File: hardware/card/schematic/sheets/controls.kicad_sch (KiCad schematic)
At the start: 12 parts, among them SW1 KMR211NG, SW10A EVP-AKE31A, SW10B EVP-AKE31A, SW2 KMR211NG, SW3 KMR211NG, SW4 KMR211NG, SW5 KMR211NG, SW6 KMR211NG, SW7 KMR211NG, SW8 KMR211NG, SW9 EVP-AKE31A

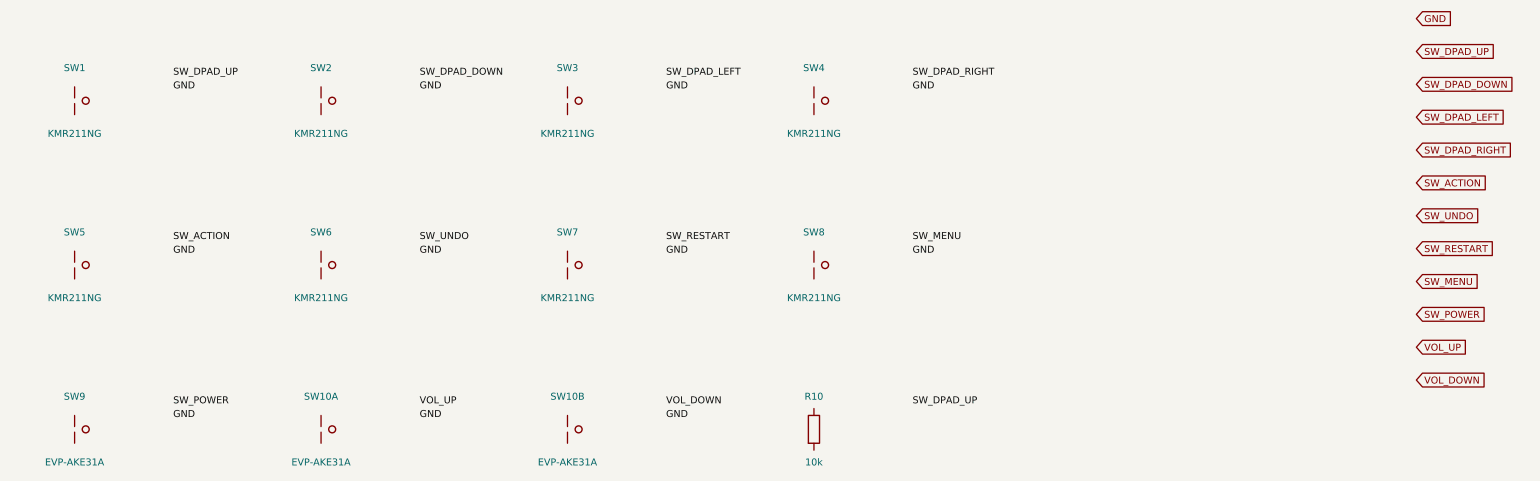
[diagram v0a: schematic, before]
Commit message: hardware: replace U7 power latch with a slide switch (hard off)
Owner-approved power model: top-edge SPDT slide switch gates the TPS63070
EN pin; hard off is the normal off (Game Boy/Arduboy style, ~1-1.5 s tuned
cold boot, end-of-level atomic saves). Deletes the U7 latch IC and SYSOFF
wiring, frees GPIO8, adds a VBUS-powered charge LED on BQ24075 CHG, and
demotes deep sleep to an optional idle battery-saver. Closes the U7
pre-route gate from the 2026-07-09 PCB review.

Co-authored-by: Cursor <cursoragent@cursor.com>
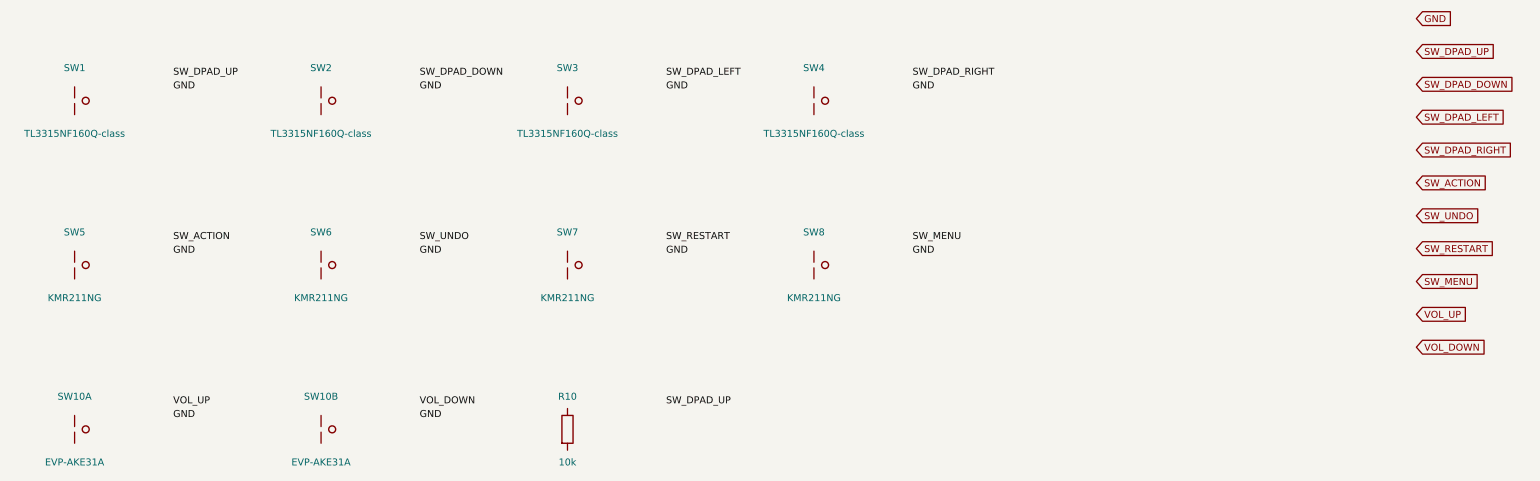
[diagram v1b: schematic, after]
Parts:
- removed SW9: EVP-AKE31A, TBD, symbol Switch:SW_Push
- SW1, SW2, SW3, SW4: value KMR211NG -> TL3315NF160Q-class
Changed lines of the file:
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@@
   (title_block
     (title "PuzzleScript Card — controls")
-    (date "2026-07-08")
+    (date "2026-07-09")
     (rev "spin1")
     (comment 1 "Auto-generated from connectivity.json")
@@
     (property "Reference" "SW1" (at 35 29 0)
       (effects (font (size 1.27 1.27))))
-    (property "Value" "KMR211NG" (at 35 41 0)
+    (property "Value" "TL3315NF160Q-class" (at 35 41 0)
       (effects (font (size 1.27 1.27))))
     (property "Footprint" "TBD" (at 35 35 0)
@@
     (property "Reference" "SW2" (at 80 29 0)
       (effects (font (size 1.27 1.27))))
-    (property "Value" "KMR211NG" (at 80 41 0)
+    (property "Value" "TL3315NF160Q-class" (at 80 41 0)
       (effects (font (size 1.27 1.27))))
     (property "Footprint" "TBD" (at 80 35 0)
@@
     (property "Reference" "SW3" (at 125 29 0)
       (effects (font (size 1.27 1.27))))
-    (property "Value" "KMR211NG" (at 125 41 0)
+    (property "Value" "TL3315NF160Q-class" (at 125 41 0)
       (effects (font (size 1.27 1.27))))
     (property "Footprint" "TBD" (at 125 35 0)
@@
     (property "Reference" "SW4" (at 170 29 0)
       (effects (font (size 1.27 1.27))))
-    (property "Value" "KMR211NG" (at 170 41 0)
+    (property "Value" "TL3315NF160Q-class" (at 170 41 0)
       (effects (font (size 1.27 1.27))))
     (property "Footprint" "TBD" (at 170 35 0)
@@
   (symbol (lib_id "Switch:SW_Push") (at 35 95 0) (unit 1)
     (exclude_from_sim no) (in_bom yes) (on_board yes) (dnp no) (fields_autoplaced)
-    (property "Reference" "SW9" (at 35 89 0)
+    (property "Reference" "SW10A" (at 35 89 0)
       (effects (font (size 1.27 1.27))))
     (property "Value" "EVP-AKE31A" (at 35 101 0)
@@
     (property "Datasheet" "~" (at 35 95 0)
       (effects (font (size 1.27 1.27)) hide))
-    (instances (project "card" (path "/card/sheets/controls" (reference "SW9") (unit 1))))
+    (instances (project "card" (path "/card/sheets/controls" (reference "SW10A") (unit 1))))
   )
   (label "GND" (at 53 92.5 0) (fields_autoplaced)
     (effects (font (size 1.27 1.27)) (justify left)))
-  (label "SW_POWER" (at 53 90 0) (fields_autoplaced)
+  (label "VOL_UP" (at 53 90 0) (fields_autoplaced)
     (effects (font (size 1.27 1.27)) (justify left)))
   (symbol (lib_id "Switch:SW_Push") (at 80 95 0) (unit 1)
     (exclude_from_sim no) (in_bom yes) (on_board yes) (dnp no) (fields_autoplaced)
-    (property "Reference" "SW10A" (at 80 89 0)
+    (property "Reference" "SW10B" (at 80 89 0)
       (effects (font (size 1.27 1.27))))
     (property "Value" "EVP-AKE31A" (at 80 101 0)
@@
     (property "Datasheet" "~" (at 80 95 0)
       (effects (font (size 1.27 1.27)) hide))
-    (instances (project "card" (path "/card/sheets/controls" (reference "SW10A") (unit 1))))
+    (instances (project "card" (path "/card/sheets/controls" (reference "SW10B") (unit 1))))
   )
   (label "GND" (at 98 92.5 0) (fields_autoplaced)
     (effects (font (size 1.27 1.27)) (justify left)))
-  (label "VOL_UP" (at 98 90 0) (fields_autoplaced)
-    (effects (font (size 1.27 1.27)) (justify left)))
-  (symbol (lib_id "Switch:SW_Push") (at 125 95 0) (unit 1)
-    (exclude_from_sim no) (in_bom yes) (on_board yes) (dnp no) (fields_autoplaced)
-    (property "Reference" "SW10B" (at 125 89 0)
-      (effects (font (size 1.27 1.27))))
-    (property "Value" "EVP-AKE31A" (at 125 101 0)
-      (effects (font (size 1.27 1.27))))
-    (property "Footprint" "TBD" (at 125 95 0)
+  (label "VOL_DOWN" (at 98 90 0) (fields_autoplaced)
+    (effects (font (size 1.27 1.27)) (justify left)))
+  (symbol (lib_id "Device:R") (at 125 95 0) (unit 1)
+    (exclude_from_sim no) (in_bom yes) (on_board yes) (dnp no) (fields_autoplaced)
+    (property "Reference" "R10" (at 125 89 0)
+      (effects (font (size 1.27 1.27))))
+    (property "Value" "10k" (at 125 101 0)
+      (effects (font (size 1.27 1.27))))
+    (property "Footprint" "0402" (at 125 95 0)
       (effects (font (size 1.27 1.27)) hide))
     (property "Datasheet" "~" (at 125 95 0)
       (effects (font (size 1.27 1.27)) hide))
-    (instances (project "card" (path "/card/sheets/controls" (reference "SW10B") (unit 1))))
-  )
-  (label "GND" (at 143 92.5 0) (fields_autoplaced)
-    (effects (font (size 1.27 1.27)) (justify left)))
-  (label "VOL_DOWN" (at 143 90 0) (fields_autoplaced)
-    (effects (font (size 1.27 1.27)) (justify left)))
-  (symbol (lib_id "Device:R") (at 170 95 0) (unit 1)
-    (exclude_from_sim no) (in_bom yes) (on_board yes) (dnp no) (fields_autoplaced)
-    (property "Reference" "R10" (at 170 89 0)
-      (effects (font (size 1.27 1.27))))
-    (property "Value" "10k" (at 170 101 0)
-      (effects (font (size 1.27 1.27))))
-    (property "Footprint" "0402" (at 170 95 0)
-      (effects (font (size 1.27 1.27)) hide))
-    (property "Datasheet" "~" (at 170 95 0)
-      (effects (font (size 1.27 1.27)) hide))
     (instances (project "card" (path "/card/sheets/controls" (reference "R10") (unit 1))))
   )
-  (label "SW_DPAD_UP" (at 188 90 0) (fields_autoplaced)
+  (label "SW_DPAD_UP" (at 143 90 0) (fields_autoplaced)
     (effects (font (size 1.27 1.27)) (justify left)))
   (global_label "GND" (shape input) (at 280 20 0) (fields_autoplaced)
@@
       (effects (font (size 1.27 1.27)) hide))
   )
-  (global_label "SW_POWER" (shape input) (at 280 74 0) (fields_autoplaced)
+  (global_label "VOL_UP" (shape input) (at 280 74 0) (fields_autoplaced)
     (effects (font (size 1.27 1.27)) (justify left))
     (property "Intersheetrefs" "${INTERSHEET_REFS}" (at 280 74 0)
       (effects (font (size 1.27 1.27)) hide))
   )
-  (global_label "VOL_UP" (shape input) (at 280 80 0) (fields_autoplaced)
+  (global_label "VOL_DOWN" (shape input) (at 280 80 0) (fields_autoplaced)
     (effects (font (size 1.27 1.27)) (justify left))
     (property "Intersheetrefs" "${INTERSHEET_REFS}" (at 280 80 0)
       (effects (font (size 1.27 1.27)) hide))
   )
-  (global_label "VOL_DOWN" (shape input) (at 280 86 0) (fields_autoplaced)
-    (effects (font (size 1.27 1.27)) (justify left))
-    (property "Intersheetrefs" "${INTERSHEET_REFS}" (at 280 86 0)
-      (effects (font (size 1.27 1.27)) hide))
-  )
